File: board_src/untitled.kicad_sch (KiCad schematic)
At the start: 3 parts, among them J3 Conn_01x03, U5 DS18B20

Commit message: Wersja początkowa 9.0
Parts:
- removed J3: Conn_01x03, symbol Connector_Generic:Conn_01x03
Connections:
- net czujnik temperatury: now reaches R14.2, U5.2 (DQ)
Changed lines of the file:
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@@
 	(wire
 		(pts
-			(xy 119.38 93.98) (xy 119.38 88.9)
-		)
-		(stroke
-			(width 0)
-			(type default)
-		)
-	)
-	(wire
-		(pts
-			(xy 120.65 99.06) (xy 119.38 99.06)
-		)
-		(stroke
-			(width 0)
-			(type default)
-		)
-	)
-	(wire
-		(pts
-			(xy 111.76 96.52) (xy 120.65 96.52)
+			(xy 111.76 96.52) (xy 129.54 96.52)
 		)
 		(stroke
@@
 	(wire
 		(pts
-			(xy 119.38 99.06) (xy 119.38 101.6)
-		)
-		(stroke
-			(width 0)
-			(type default)
-		)
-	)
-	(wire
-		(pts
-			(xy 120.65 93.98) (xy 119.38 93.98)
-		)
-		(stroke
-			(width 0)
-			(type default)
-		)
-	)
-	(wire
-		(pts
 			(xy 111.76 93.98) (xy 111.76 96.52)
 		)
@@
 			(width 0)
 			(type default)
+		)
+	)
+	(hierarchical_label "czujnik temperatury"
+		(shape input)
+		(at 129.54 96.52 0)
+		(effects
+			(font
+				(size 1.27 1.27)
+			)
+			(justify left)
 		)
 	)
@@
 	)
 	(symbol
-		(lib_id "Connector_Generic:Conn_01x03")
-		(at 125.73 96.52 0)
-		(unit 1)
-		(exclude_from_sim no)
-		(in_bom yes)
-		(on_board yes)
-		(dnp no)
-		(fields_autoplaced yes)
-		(property "Reference" "J3"
-			(at 128.27 95.2499 0)
-			(effects
-				(font
-					(size 1.27 1.27)
-				)
-				(justify left)
-			)
-		)
-		(property "Value" "Conn_01x03"
-			(at 128.27 97.7899 0)
-			(effects
-				(font
-					(size 1.27 1.27)
-				)
-				(justify left)
-			)
-		)
-		(property "Footprint" ""
-			(at 125.73 96.52 0)
-			(effects
-				(font
-					(size 1.27 1.27)
-				)
-				(hide yes)
-			)
-		)
-		(property "Datasheet" "~"
-			(at 125.73 96.52 0)
-			(effects
-				(font
-					(size 1.27 1.27)
-				)
-				(hide yes)
-			)
-		)
-		(property "Description" "Generic connector, single row, 01x03, script generated (kicad-library-utils/schlib/autogen/connector/)"
-			(at 125.73 96.52 0)
-			(effects
-				(font
-					(size 1.27 1.27)
-				)
-				(hide yes)
-			)
-		)
-		(pin "3"
-		)
-		(pin "2"
-		)
-		(pin "1"
-		)
-		(instances
-			(project "board"
-				(path "/772e9f49-cfcf-4cf6-843d-0684684f2d4b/4ce4dd53-34e3-426c-821d-561d412e5bd5"
-					(reference "J3")
-					(unit 1)
-				)
-			)
-		)
-	)
-	(symbol
 		(lib_id "power:GND")
 		(at 102.87 106.68 0)
@@
 					(unit 1)
 				)
-			)
-		)
-	)
-	(symbol
-		(lib_id "power:GND")
-		(at 119.38 101.6 0)
-		(unit 1)
-		(exclude_from_sim no)
-		(in_bom yes)
-		(on_board yes)
-		(dnp no)
-		(fields_autoplaced yes)
-		(property "Reference" "#PWR019"
-			(at 119.38 107.95 0)
-			(effects
-				(font
-					(size 1.27 1.27)
-				)
-				(hide yes)
-			)
-		)
-		(property "Value" "GND"
-			(at 119.38 106.68 0)
-			(effects
-				(font
-					(size 1.27 1.27)
-				)
-			)
-		)
-		(property "Footprint" ""
-			(at 119.38 101.6 0)
-			(effects
-				(font
-					(size 1.27 1.27)
-				)
-				(hide yes)
-			)
-		)
-		(property "Datasheet" ""
-			(at 119.38 101.6 0)
-			(effects
-				(font
-					(size 1.27 1.27)
-				)
-				(hide yes)
-			)
-		)
-		(property "Description" "Power symbol creates a global label with name \"GND\" , ground"
-			(at 119.38 101.6 0)
-			(effects
-				(font
-					(size 1.27 1.27)
-				)
-				(hide yes)
-			)
-		)
-		(pin "1"
-		)
-		(instances
-			(project "board"
-				(path "/772e9f49-cfcf-4cf6-843d-0684684f2d4b/4ce4dd53-34e3-426c-821d-561d412e5bd5"
-					(reference "#PWR019")
-					(unit 1)
-				)
-			)
-		)
-	)
-	(symbol
-		(lib_id "power:+3.3V")
-		(at 119.38 88.9 0)
-		(unit 1)
-		(exclude_from_sim no)
-		(in_bom yes)
-		(on_board yes)
-		(dnp no)
-		(fields_autoplaced yes)
-		(property "Reference" "#PWR018"
-			(at 119.38 92.71 0)
-			(effects
-				(font
-					(size 1.27 1.27)
-				)
-				(hide yes)
-			)
-		)
-		(property "Value" "+3.3V"
-			(at 119.38 83.82 0)
-			(effects
-				(font
-					(size 1.27 1.27)
-				)
-			)
-		)
-		(property "Footprint" ""
-			(at 119.38 88.9 0)
-			(effects
-				(font
-					(size 1.27 1.27)
-				)
-				(hide yes)
-			)
-		)
-		(property "Datasheet" ""
-			(at 119.38 88.9 0)
-			(effects
-				(font
-					(size 1.27 1.27)
-				)
-				(hide yes)
-			)
-		)
-		(property "Description" "Power symbol creates a global label with name \"+3.3V\""
-			(at 119.38 88.9 0)
-			(effects
-				(font
-					(size 1.27 1.27)
-				)
-				(hide yes)
-			)
-		)
-		(pin "1"
-		)
-		(instances
-			(project "board"
-				(path "/772e9f49-cfcf-4cf6-843d-0684684f2d4b/4ce4dd53-34e3-426c-821d-561d412e5bd5"
-					(reference "#PWR018")
-					(unit 1)
-				)

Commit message: wersja dodane arkusze hierarchiczne
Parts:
- removed R14: 103, Resistor_SMD:R_0201_0603Metric, symbol Device:R
- removed U5: DS18B20, Package_TO_SOT_THT:TO-92_Inline, symbol Sensor_Temperature:DS18B20
- added IC3: DS18B20+, DS18B20, symbol DS18B20+:DS18B20+
- added J11: Conn_01x03, symbol Connector_Generic:Conn_01x03
- added R19: 103, Resistor_SMD:R_0201_0603Metric, symbol Device:R
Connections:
- new net: IC3.2 (DQ), J11.2 (Pin_2), R19.1
- new net 3,3V: IC3.3 (VDD), J11.1 (Pin_1), R19.2
- new net gnd: IC3.1 (GND), J11.3 (Pin_3)
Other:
- note removed: "czujnik temperatury"

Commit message: wersja dodane arkusze hierarchiczne
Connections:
- net 3,3V renamed +3.3V
- net gnd renamed GND
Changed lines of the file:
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@@
-	(wire
-		(pts
-			(xy 186.69 81.28) (xy 186.69 87.63)
-		)
-		(stroke
-			(width 0)
-			(type default)
-		)
-	)
 	(wire
 		(pts
@@
 	(wire
 		(pts
+			(xy 186.69 80.01) (xy 186.69 87.63)
+		)
+		(stroke
+			(width 0)
+			(type default)
+		)
+	)
+	(wire
+		(pts
 			(xy 148.59 107.95) (xy 149.86 107.95)
 		)
@@
 	(wire
 		(pts
-			(xy 186.69 138.43) (xy 180.34 138.43)
-		)
-		(stroke
-			(width 0)
-			(type default)
-		)
-	)
-	(wire
-		(pts
 			(xy 186.69 87.63) (xy 186.69 106.68)
 		)
@@
 	(wire
 		(pts
-			(xy 186.69 138.43) (xy 186.69 133.35)
+			(xy 186.69 133.35) (xy 186.69 139.7)
 		)
 		(stroke
@@
 		)
 	)
-	(global_label "gnd"
-		(shape input)
-		(at 186.69 81.28 180)
+	(symbol
+		(lib_id "power:+3.3V")
+		(at 186.69 139.7 180)
+		(unit 1)
+		(exclude_from_sim no)
+		(in_bom yes)
+		(on_board yes)
+		(dnp no)
 		(fields_autoplaced yes)
-		(effects
-			(font
-				(size 1.27 1.27)
-			)
-			(justify right)
-		)
-		(property "Intersheetrefs" "${INTERSHEET_REFS}"
-			(at 180.2578 81.28 0)
-			(effects
-				(font
-					(size 1.27 1.27)
-				)
-				(justify right)
-				(hide yes)
-			)
-		)
-	)
-	(global_label "3,3V"
-		(shape input)
-		(at 180.34 138.43 180)
+		(property "Reference" "#PWR016"
+			(at 186.69 135.89 0)
+			(effects
+				(font
+					(size 1.27 1.27)
+				)
+				(hide yes)
+			)
+		)
+		(property "Value" "+3.3V"
+			(at 186.69 144.78 0)
+			(effects
+				(font
+					(size 1.27 1.27)
+				)
+			)
+		)
+		(property "Footprint" ""
+			(at 186.69 139.7 0)
+			(effects
+				(font
+					(size 1.27 1.27)
+				)
+				(hide yes)
+			)
+		)
+		(property "Datasheet" ""
+			(at 186.69 139.7 0)
+			(effects
+				(font
+					(size 1.27 1.27)
+				)
+				(hide yes)
+			)
+		)
+		(property "Description" "Power symbol creates a global label with name \"+3.3V\""
+			(at 186.69 139.7 0)
+			(effects
+				(font
+					(size 1.27 1.27)
+				)
+				(hide yes)
+			)
+		)
+		(pin "1"
+		)
+		(instances
+			(project "board"
+				(path "/772e9f49-cfcf-4cf6-843d-0684684f2d4b/4ce4dd53-34e3-426c-821d-561d412e5bd5"
+					(reference "#PWR016")
+					(unit 1)
+				)
+			)
+		)
+	)
+	(symbol
+		(lib_id "power:GND")
+		(at 186.69 80.01 180)
+		(unit 1)
+		(exclude_from_sim no)
+		(in_bom yes)
+		(on_board yes)
+		(dnp no)
 		(fields_autoplaced yes)
-		(effects
-			(font
-				(size 1.27 1.27)
-			)
-			(justify right)
-		)
-		(property "Intersheetrefs" "${INTERSHEET_REFS}"
-			(at 173.2424 138.43 0)
-			(effects
-				(font
-					(size 1.27 1.27)
-				)
-				(justify right)
-				(hide yes)
-			)
-		)
+		(property "Reference" "#PWR04"
+			(at 186.69 73.66 0)
+			(effects
+				(font
+					(size 1.27 1.27)
+				)
+				(hide yes)
+			)
+		)
+		(property "Value" "GND"
+			(at 186.69 74.93 0)
+			(effects
+				(font
+					(size 1.27 1.27)
+				)
+			)
+		)
+		(property "Footprint" ""
+			(at 186.69 80.01 0)
+			(effects
+				(font
+					(size 1.27 1.27)
+				)
+				(hide yes)
+			)
+		)
+		(property "Datasheet" ""
+			(at 186.69 80.01 0)
+			(effects
+				(font
+					(size 1.27 1.27)
+				)
+				(hide yes)
+			)
+		)
+		(property "Description" "Power symbol creates a global label with name \"GND\" , ground"
+			(at 186.69 80.01 0)
+			(effects
+				(font
+					(size 1.27 1.27)
+				)
+				(hide yes)
+			)
+		)
+		(pin "1"
+		)
+		(instances
+			(project ""
+				(path "/772e9f49-cfcf-4cf6-843d-0684684f2d4b/4ce4dd53-34e3-426c-821d-561d412e5bd5"
+					(reference "#PWR04")
+					(unit 1)
+				)
+			)
+		)

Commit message: wersja uzupelnione footprinty
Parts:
- IC3: footprint DS18B20 -> footprints:DS18B20
- J11: footprint (none) -> Connector_PinHeader_2.54mm:PinHeader_1x03_P2.54mm_Vertical
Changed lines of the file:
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@@
 			)
 		)
-		(property "Footprint" ""
+		(property "Footprint" "Connector_PinHeader_2.54mm:PinHeader_1x03_P2.54mm_Vertical"
 			(at 143.51 110.49 0)
 			(effects
@@
 			)
 		)
-		(property "Footprint" "DS18B20"
+		(property "Footprint" "footprints:DS18B20"
 			(at 205.74 201.6 0)
 			(effects

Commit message: wersja 3d
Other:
- note added: "Jaka wartość opornika?"
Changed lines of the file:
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@@
 	(generator_version "9.0")
 	(paper "A4")
+	(text "Jaka wartość opornika?\n"
+		(exclude_from_sim no)
+		(at 172.212 122.682 0)
+		(effects
+			(font
+				(size 1.27 1.27)
+			)
+		)
+	)
 	(junction
 		(at 186.69 133.35)

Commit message: wersja z FT232RN
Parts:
- R19: value 103 -> 10k; footprint Resistor_SMD:R_0201_0603Metric -> Resistor_SMD:R_1206_3216Metric
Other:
- title: (none) -> czujnik
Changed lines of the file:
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@@
 	(generator_version "9.0")
 	(paper "A4")
+	(title_block
+		(title "czujnik")
+	)
 	(text "Jaka wartość opornika?\n"
 		(exclude_from_sim no)
@@
 			)
 		)
-		(property "Value" "103"
+		(property "Value" "10k"
 			(at 175.768 116.586 0)
 			(effects
@@
 			)
 		)
-		(property "Footprint" "Resistor_SMD:R_0201_0603Metric"
+		(property "Footprint" "Resistor_SMD:R_1206_3216Metric"
 			(at 175.26 119.888 90)
 			(effects

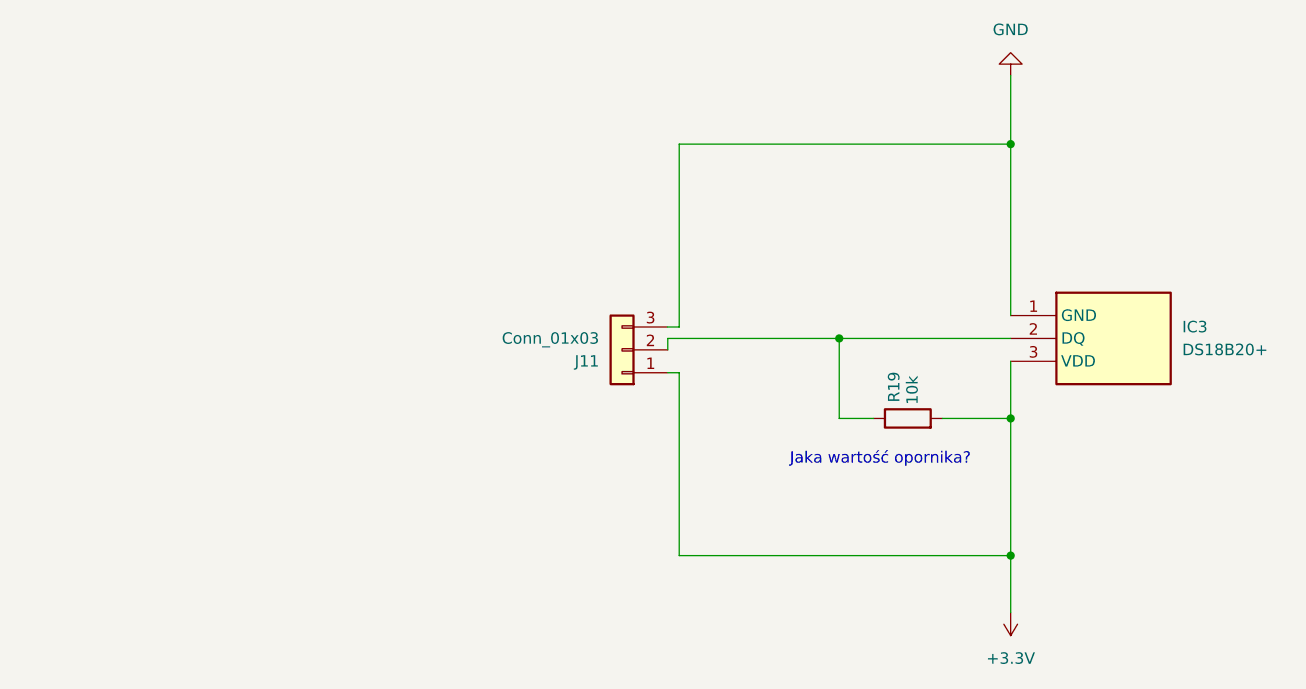
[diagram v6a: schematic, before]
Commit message: Wersja ze sciezkami miedzianymi
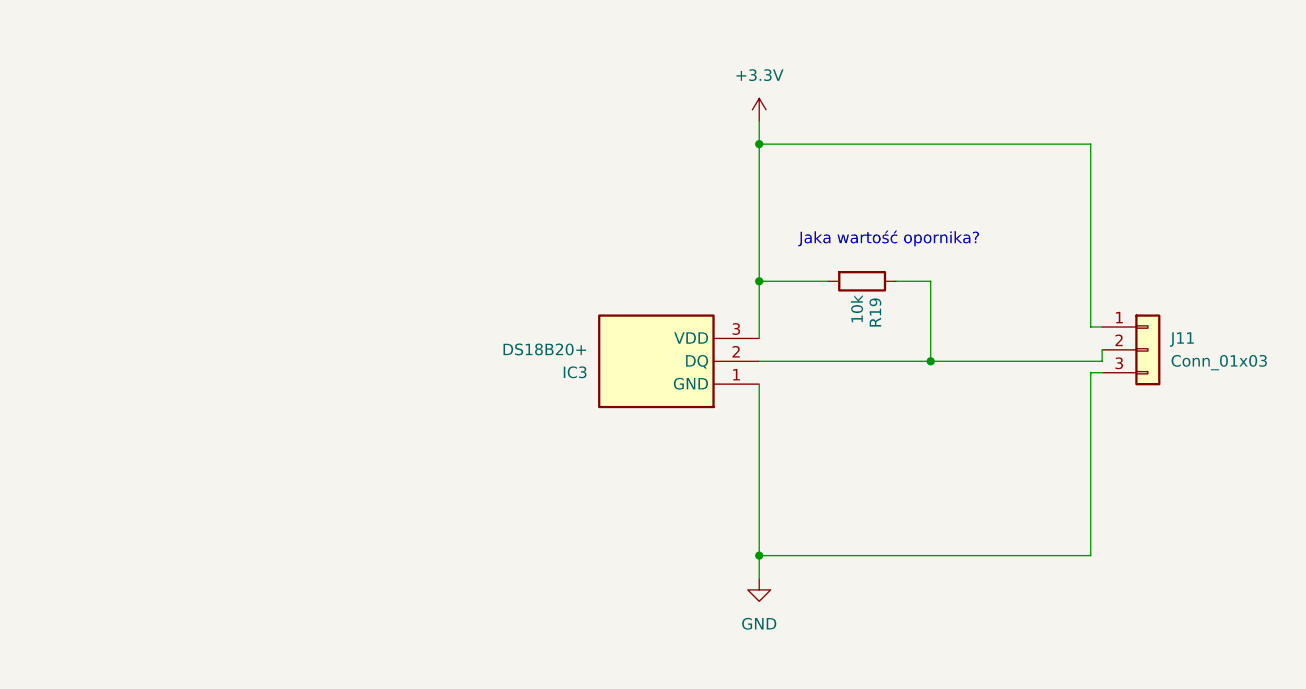
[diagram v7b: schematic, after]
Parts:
- R19: footprint Resistor_SMD:R_1206_3216Metric -> Resistor_SMD:R_0603_1608Metric
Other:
- moved on the sheet: IC3, J11, R19

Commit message: poprawione polaczenia diod i wartosci opornikow, aktualizacja niektorych elementow ze wzgledu na braki w magazynie
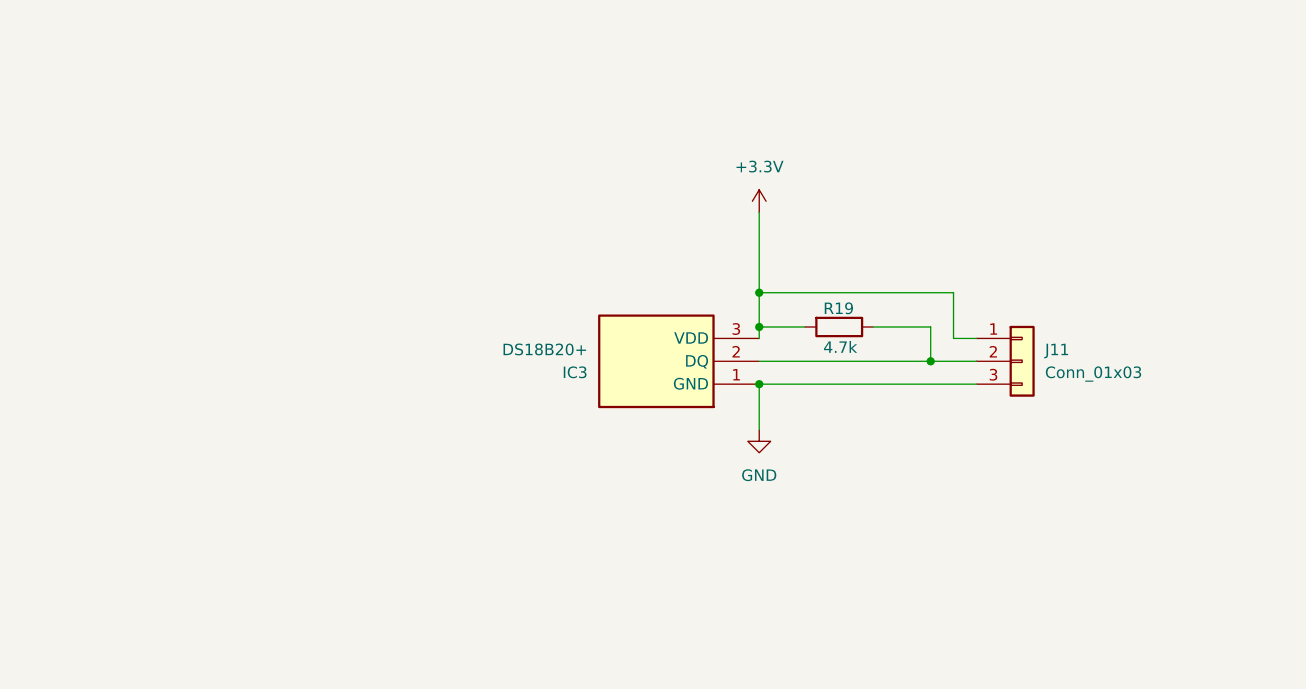
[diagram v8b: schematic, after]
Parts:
- R19: value 10k -> 4.7k
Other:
- note removed: "Jaka wartość opornika?"
- moved on the sheet: J11, R19
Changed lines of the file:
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@@
 		(title "czujnik")
 	)
-	(text "Jaka wartość opornika?\n"
-		(exclude_from_sim no)
-		(at 173.228 98.298 0)
-		(effects
-			(font
-				(size 1.27 1.27)
-			)
-		)
-	)
 	(junction
-		(at 158.75 87.63)
-		(diameter 0)
-		(color 0 0 0 0)
-	)
-	(junction
-		(at 158.75 133.35)
-		(diameter 0)
-		(color 0 0 0 0)
-	)
-	(junction
-		(at 158.75 102.87)
+		(at 158.75 104.14)
 		(diameter 0)
 		(color 0 0 0 0)
@@
 		(color 0 0 0 0)
 	)
+	(junction
+		(at 158.75 107.95)
+		(diameter 0)
+		(color 0 0 0 0)
+	)
+	(junction
+		(at 158.75 114.3)
+		(diameter 0)
+		(color 0 0 0 0)
+	)
 	(wire
 		(pts
@@
 	(wire
 		(pts
-			(xy 195.58 107.95) (xy 195.58 87.63)
-		)
-		(stroke
-			(width 0)
-			(type default)
-		)
-	)
-	(wire
-		(pts
-			(xy 158.75 135.89) (xy 158.75 133.35)
-		)
-		(stroke
-			(width 0)
-			(type default)
-		)
-	)
-	(wire
-		(pts
-			(xy 196.85 113.03) (xy 195.58 113.03)
-		)
-		(stroke
-			(width 0)
-			(type default)
-		)
-	)
-	(wire
-		(pts
-			(xy 173.99 102.87) (xy 177.8 102.87)
-		)
-		(stroke
-			(width 0)
-			(type default)
-		)
-	)
-	(wire
-		(pts
-			(xy 166.37 102.87) (xy 158.75 102.87)
-		)
-		(stroke
-			(width 0)
-			(type default)
-		)
-	)
-	(wire
-		(pts
-			(xy 196.85 111.76) (xy 177.8 111.76)
-		)
-		(stroke
-			(width 0)
-			(type default)
-		)
-	)
-	(wire
-		(pts
-			(xy 196.85 107.95) (xy 195.58 107.95)
-		)
-		(stroke
-			(width 0)
-			(type default)
-		)
-	)
-	(wire
-		(pts
-			(xy 158.75 133.35) (xy 158.75 114.3)
-		)
-		(stroke
-			(width 0)
-			(type default)
-		)
-	)
-	(wire
-		(pts
-			(xy 177.8 102.87) (xy 177.8 111.76)
-		)
-		(stroke
-			(width 0)
-			(type default)
-		)
-	)
-	(wire
-		(pts
-			(xy 196.85 111.76) (xy 196.85 110.49)
-		)
-		(stroke
-			(width 0)
-			(type default)
-		)
-	)
-	(wire
-		(pts
-			(xy 158.75 109.22) (xy 158.75 102.87)
-		)
-		(stroke
-			(width 0)
-			(type default)
-		)
-	)
-	(wire
-		(pts
-			(xy 195.58 133.35) (xy 158.75 133.35)
-		)
-		(stroke
-			(width 0)
-			(type default)
-		)
-	)
-	(wire
-		(pts
-			(xy 195.58 133.35) (xy 195.58 113.03)
-		)
-		(stroke
-			(width 0)
-			(type default)
-		)
-	)
-	(wire
-		(pts
-			(xy 195.58 87.63) (xy 158.75 87.63)
-		)
-		(stroke
-			(width 0)
-			(type default)
-		)
-	)
-	(wire
-		(pts
-			(xy 158.75 87.63) (xy 158.75 85.09)
-		)
-		(stroke
-			(width 0)
-			(type default)
-		)
-	)
-	(wire
-		(pts
-			(xy 158.75 102.87) (xy 158.75 87.63)
+			(xy 180.34 109.22) (xy 180.34 104.14)
+		)
+		(stroke
+			(width 0)
+			(type default)
+		)
+	)
+	(wire
+		(pts
+			(xy 171.45 107.95) (xy 177.8 107.95)
+		)
+		(stroke
+			(width 0)
+			(type default)
+		)
+	)
+	(wire
+		(pts
+			(xy 163.83 107.95) (xy 158.75 107.95)
+		)
+		(stroke
+			(width 0)
+			(type default)
+		)
+	)
+	(wire
+		(pts
+			(xy 182.88 111.76) (xy 177.8 111.76)
+		)
+		(stroke
+			(width 0)
+			(type default)
+		)
+	)
+	(wire
+		(pts
+			(xy 158.75 104.14) (xy 158.75 107.95)
+		)
+		(stroke
+			(width 0)
+			(type default)
+		)
+	)
+	(wire
+		(pts
+			(xy 182.88 109.22) (xy 180.34 109.22)
+		)
+		(stroke
+			(width 0)
+			(type default)
+		)
+	)
+	(wire
+		(pts
+			(xy 158.75 114.3) (xy 158.75 119.38)
+		)
+		(stroke
+			(width 0)
+			(type default)
+		)
+	)
+	(wire
+		(pts
+			(xy 177.8 107.95) (xy 177.8 111.76)
+		)
+		(stroke
+			(width 0)
+			(type default)
+		)
+	)
+	(wire
+		(pts
+			(xy 158.75 109.22) (xy 158.75 107.95)
+		)
+		(stroke
+			(width 0)
+			(type default)
+		)
+	)
+	(wire
+		(pts
+			(xy 158.75 114.3) (xy 182.88 114.3)
+		)
+		(stroke
+			(width 0)
+			(type default)
+		)
+	)
+	(wire
+		(pts
+			(xy 158.75 95.25) (xy 158.75 104.14)
+		)
+		(stroke
+			(width 0)
+			(type default)
+		)
+	)
+	(wire
+		(pts
+			(xy 180.34 104.14) (xy 158.75 104.14)
 		)
 		(stroke
@@
 	(symbol
 		(lib_id "power:+3.3V")
-		(at 158.75 85.09 0)
+		(at 158.75 95.25 0)
 		(unit 1)
 		(exclude_from_sim no)
@@
 		(fields_autoplaced yes)
 		(property "Reference" "#PWR016"
-			(at 158.75 88.9 0)
+			(at 158.75 99.06 0)
 			(effects
 				(font
@@
 		)
 		(property "Value" "+3.3V"
-			(at 158.75 80.01 0)
+			(at 158.75 90.17 0)
 			(effects
 				(font
@@
 		)
 		(property "Footprint" ""
-			(at 158.75 85.09 0)
+			(at 158.75 95.25 0)
 			(effects
 				(font
@@
 		)
 		(property "Datasheet" ""
-			(at 158.75 85.09 0)
+			(at 158.75 95.25 0)
 			(effects
 				(font
@@
 		)
 		(property "Description" "Power symbol creates a global label with name \"+3.3V\""
-			(at 158.75 85.09 0)
+			(at 158.75 95.25 0)
 			(effects
 				(font
@@
 	(symbol
 		(lib_id "power:GND")
-		(at 158.75 135.89 0)
+		(at 158.75 119.38 0)
 		(unit 1)
 		(exclude_from_sim no)
@@
 		(fields_autoplaced yes)
 		(property "Reference" "#PWR04"
-			(at 158.75 142.24 0)
+			(at 158.75 125.73 0)
 			(effects
 				(font
@@
 		)
 		(property "Value" "GND"
-			(at 158.75 140.97 0)
+			(at 158.75 124.46 0)
 			(effects
 				(font
@@
 		)
 		(property "Footprint" ""
-			(at 158.75 135.89 0)
+			(at 158.75 119.38 0)
 			(effects
 				(font
@@
 		)
 		(property "Datasheet" ""
-			(at 158.75 135.89 0)
+			(at 158.75 119.38 0)
 			(effects
 				(font
@@
 		)
 		(property "Description" "Power symbol creates a global label with name \"GND\" , ground"
-			(at 158.75 135.89 0)
+			(at 158.75 119.38 0)
 			(effects
 				(font
@@
 	(symbol
 		(lib_id "Device:R")
-		(at 170.18 102.87 270)
+		(at 167.64 107.95 270)
 		(unit 1)
 		(exclude_from_sim no)
@@
 		(dnp no)
 		(property "Reference" "R19"
-			(at 171.704 104.648 0)
+			(at 165.862 105.918 90)
 			(effects
 				(font
@@
 			)
 		)
-		(property "Value" "10k"
-			(at 169.672 104.394 0)
+		(property "Value" "4.7k"
+			(at 165.862 110.236 90)
 			(effects
 				(font
@@
 		)
 		(property "Footprint" "Resistor_SMD:R_0603_1608Metric"
-			(at 170.18 101.092 90)
+			(at 167.64 106.172 90)
 			(effects
 				(font
@@
 		)
 		(property "Datasheet" "~"
-			(at 170.18 102.87 0)
+			(at 167.64 107.95 0)
 			(effects
 				(font
@@
 		)
 		(property "Description" "Resistor"
-			(at 170.18 102.87 0)
+			(at 167.64 107.95 0)
 			(effects
 				(font
@@
 	(symbol
 		(lib_id "Connector_Generic:Conn_01x03")
-		(at 201.93 110.49 0)
+		(at 187.96 111.76 0)
 		(unit 1)
 		(exclude_from_sim no)
@@
 		(fields_autoplaced yes)
 		(property "Reference" "J11"
-			(at 204.47 109.2199 0)
+			(at 190.5 110.4899 0)
 			(effects
 				(font
@@
 		)
 		(property "Value" "Conn_01x03"
-			(at 204.47 111.7599 0)
+			(at 190.5 113.0299 0)
 			(effects
 				(font
@@
 		)
 		(property "Footprint" "Connector_PinHeader_2.54mm:PinHeader_1x03_P2.54mm_Vertical"
-			(at 201.93 110.49 0)
+			(at 187.96 111.76 0)
 			(effects
 				(font
@@
 		)
 		(property "Datasheet" "~"
-			(at 201.93 110.49 0)
+			(at 187.96 111.76 0)
 			(effects
 				(font
@@
 		)
 		(property "Description" "Generic connector, single row, 01x03, script generated (kicad-library-utils/schlib/autogen/connector/)"
-			(at 201.93 110.49 0)
-			(effects
-				(font
+			(at 187.96 111.76 0)
+			(effects
+				(font
